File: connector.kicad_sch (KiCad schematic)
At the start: 10 parts, among them M1 PTH_M2.5, M2 PTH_M2.5, Q1 DMG1012UW-7, Q2 DMG1012UW-7, U1 FXLA108BQX

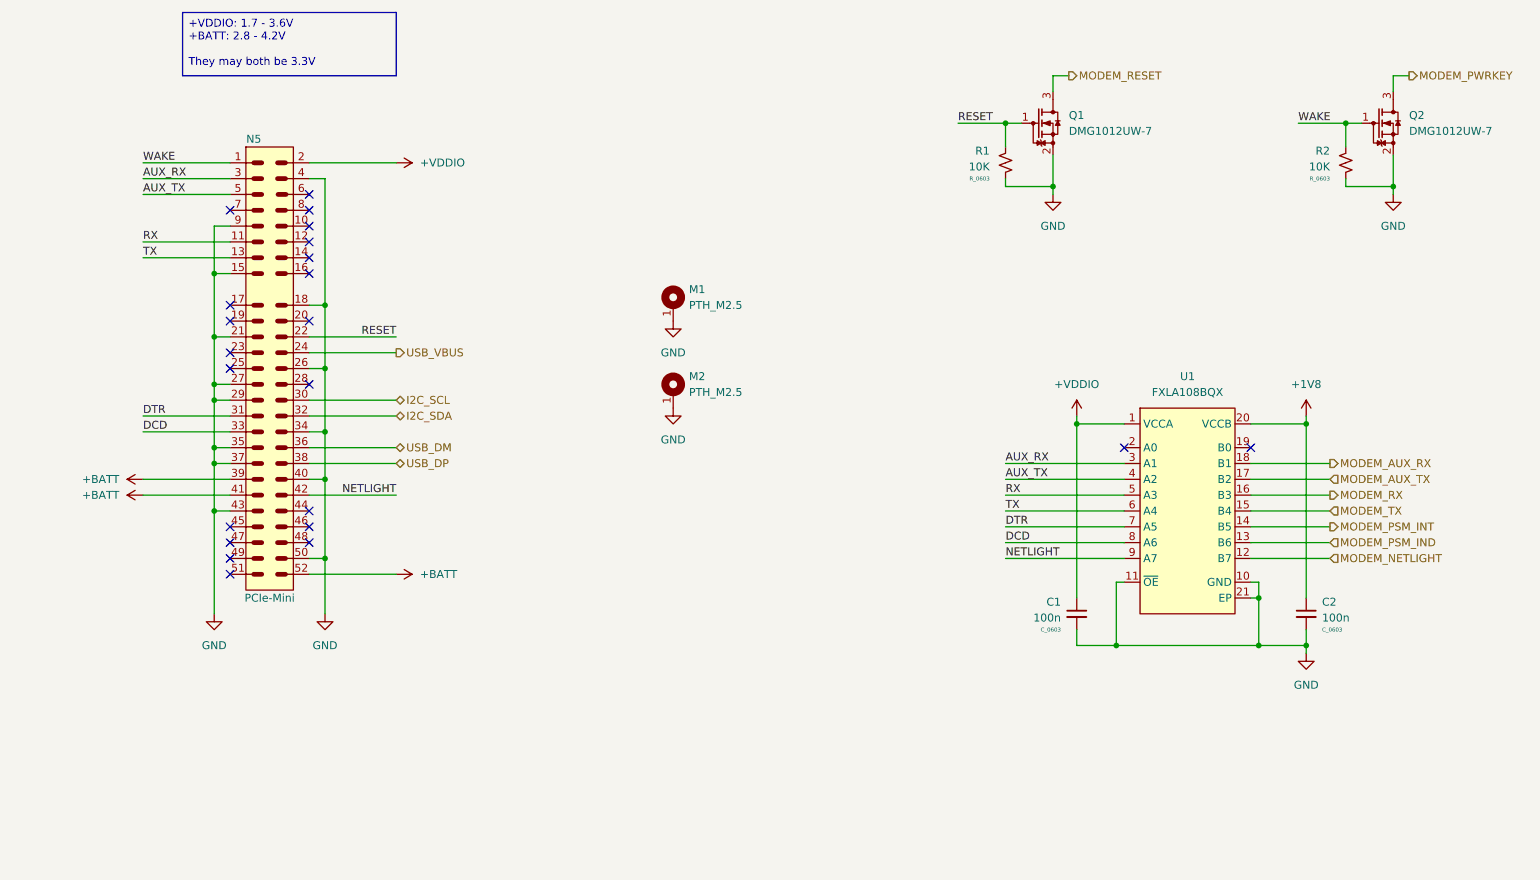
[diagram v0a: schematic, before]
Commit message: Update for DTR/DCD
Add LDO for 1v8 reference
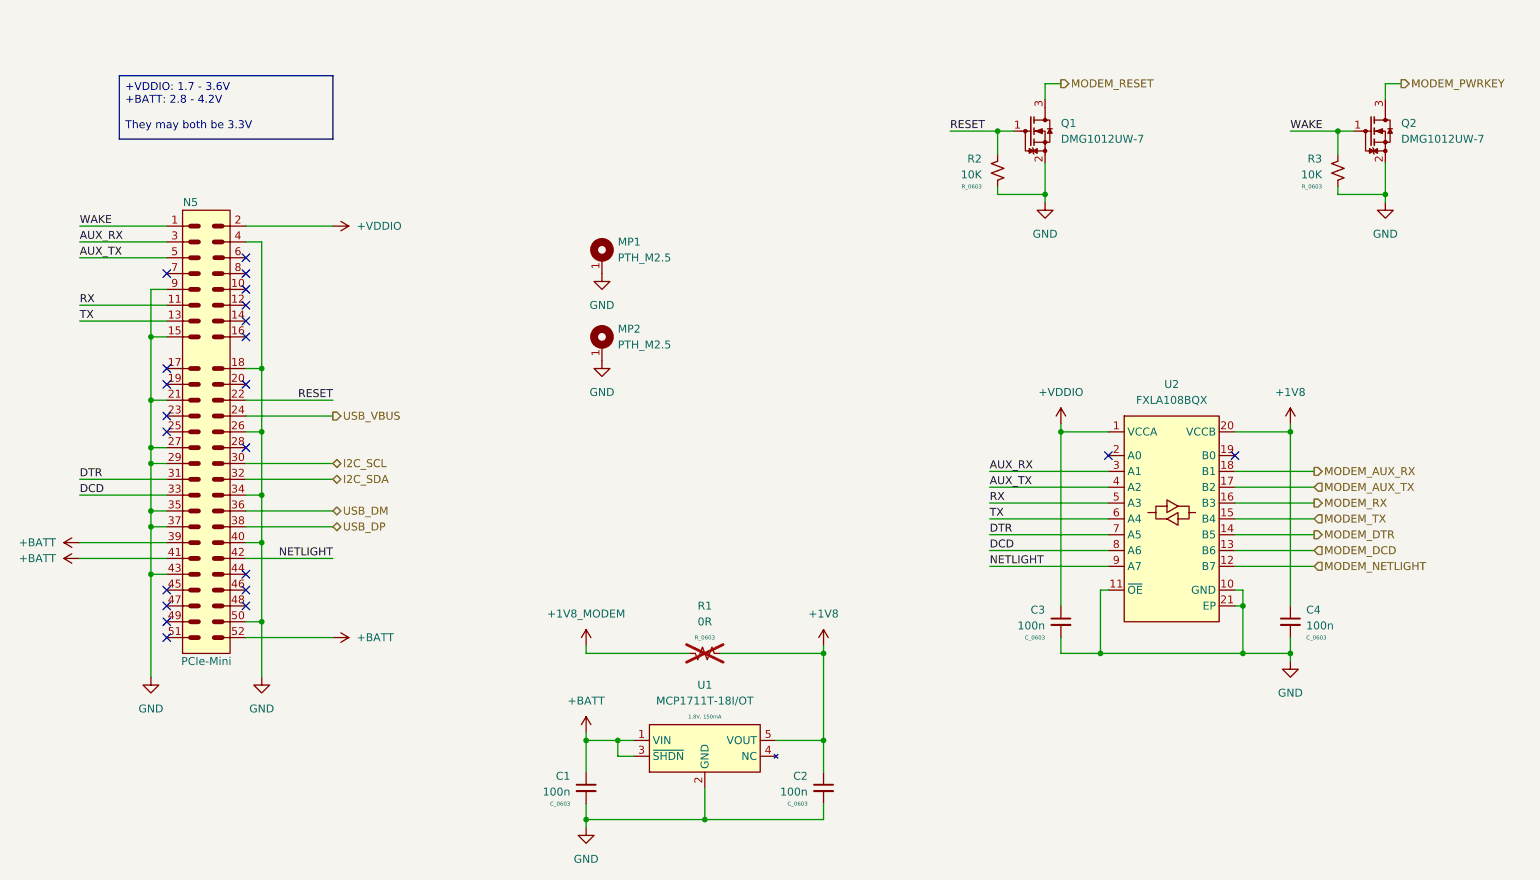
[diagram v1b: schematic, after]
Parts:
- added C1, C2: 100n, C_Capacitor:C_0603, symbol C_Capacitor:C_0603
- added R1: 0R, R_Resistor:R_0603, symbol R_Resistor:R_0603
- added U1: MCP1711T-18I/OT, U_IC:SOT23_5, symbol U_PowerLinear:MCP1711T-18I/OT
- MP1: renamed from M1; footprint M_Mechanical:PTH_M2.5 -> MP_Mechanical:PTH_M2.5; symbol M_Mechanical:PTH_M2.5 -> MP_Mechanical:PTH_M2.5
- MP2: renamed from M2; footprint M_Mechanical:PTH_M2.5 -> MP_Mechanical:PTH_M2.5; symbol M_Mechanical:PTH_M2.5 -> MP_Mechanical:PTH_M2.5
- U2: renamed from U1; symbol U_Basic:FXLA108BQX -> U_Logic:FXLA108BQX
- renumbered C1 to C3, C2 to C4, R1 to R2, R2 to R3
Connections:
- net +1V8: now also C2.1, R1.1, U1.5 (VOUT)
- net +BATT: now also C1.1, U1.1 (VIN), U1.3 (~{SHDN})
- net GND: now also C1.2, C2.2, U1.2 (GND)
- net MODEM_PSM_IND renamed MODEM_DCD
- net MODEM_PSM_INT renamed MODEM_DTR
- new net +1V8_MODEM: R1.2
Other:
- moved on the sheet: C3, C4, MP1, MP2, N5, Q1, Q2, R2, R3
